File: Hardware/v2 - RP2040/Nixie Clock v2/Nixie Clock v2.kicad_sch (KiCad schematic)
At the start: 25 parts, among them J1 USB_C_Receptacle_USB2.0, J2 Conn_01x03, SW1 SW_Push, U1 RP2040, U2 W25Q128JVS, Y1 12MHz

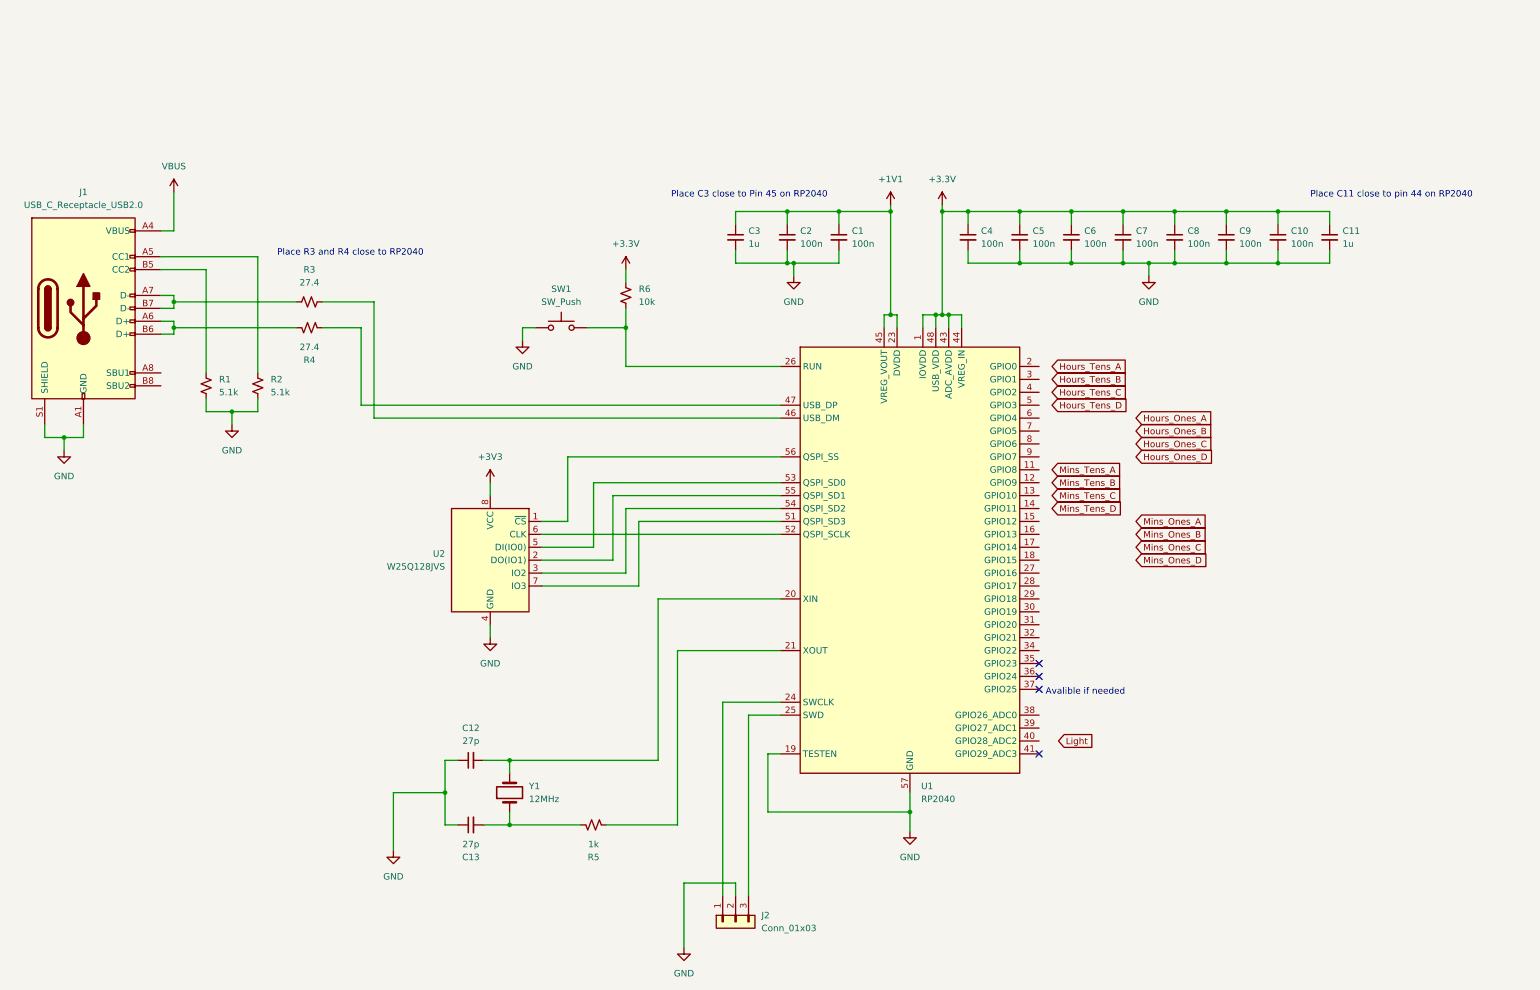
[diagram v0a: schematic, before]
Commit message: added schematic pages and HV switching circuit
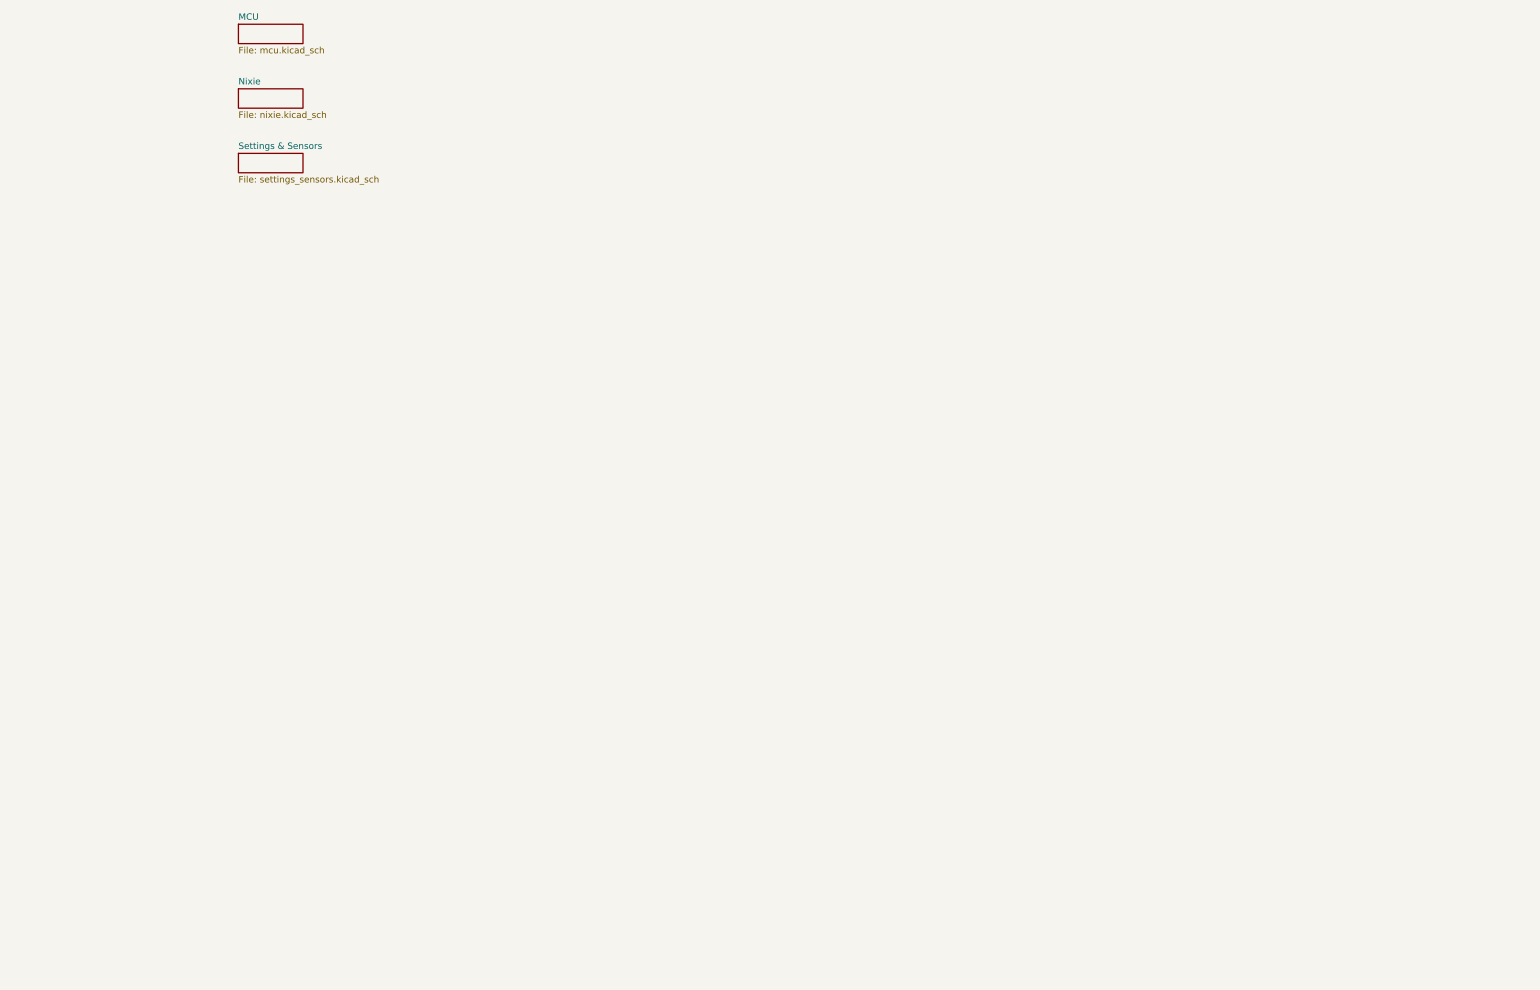
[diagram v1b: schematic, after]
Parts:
- removed C1, C10, C2, C4, C5, C6, C7, C8, C9: 100n, symbol Device:C_Small
- removed C11, C3: 1u, symbol Device:C_Small
- removed C12, C13: 27p, symbol Device:C_Small
- removed J1: USB_C_Receptacle_USB2.0, symbol Connector:USB_C_Receptacle_USB2.0
- removed J2: Conn_01x03, symbol Connector_Generic:Conn_01x03
- removed R1, R2: 5.1k, symbol Device:R_Small_US
- removed R3, R4: 27.4, symbol Device:R_Small_US
- removed R5: 1k, symbol Device:R_Small_US
- removed R6: 10k, symbol Device:R_Small_US
- removed SW1: SW_Push, symbol Switch:SW_Push
- removed U1: RP2040, Package_DFN_QFN:QFN-56-1EP_7x7mm_P0.4mm_EP3.2x3.2mm, symbol MCU_RaspberryPi:RP2040
- removed U2: W25Q128JVS, Package_SO:SOIC-8_5.23x5.23mm_P1.27mm, symbol Memory_Flash:W25Q128JVS
- removed Y1: 12MHz, symbol Device:Crystal
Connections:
- no-connect marks 4 -> 0
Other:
- added sheet MCU (mcu.kicad_sch)
- added sheet Nixie (nixie.kicad_sch)
- added sheet Settings & Sensors (settings_sensors.kicad_sch)
- note removed: "Avalible if needed"
- note removed: "Place C11 close to pin 44 on RP2040"
- note removed: "Place C3 close to Pin 45 on RP2040"
- note removed: "Place R3 and R4 close to RP2040"
- title: (none) -> Nixie Tube Clock

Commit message: Complteted schematic, mergerd schematic on to one sheet, started assigning footprints
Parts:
- added BT1: CR1220, Battery:BatteryHolder_LINX_BAT-HLD-012-SMT, symbol Device:Battery_Cell
- added C10, C11, C12, C13, C14, C15, C16, C17, C20, C21, C24, C25, C29, C3, C33, C35, C5, C9: 100n, Capacitor_SMD:C_0603_1608Metric, symbol Device:C_Small
- added C14: 100u, Capacitor_SMD:C_0603_1608Metric, symbol Device:C_Small
- added C15: 4.7u, Capacitor_THT:CP_Radial_D8.0mm_P3.50mm, symbol Device:C_Polarized_Small_US
- added C18, C19: 1u, Capacitor_SMD:C_0402_1005Metric, symbol Device:C_Small
- added C22, C23, C30, C31, C34: 1u, Capacitor_SMD:C_0603_1608Metric, symbol Device:C_Small
- added C26, C4: 10u, Capacitor_SMD:C_0603_1608Metric, symbol Device:C_Small
- added C27, C28: 27p, Capacitor_SMD:C_0603_1608Metric, symbol Device:C_Small
- added C32: 10n, Capacitor_SMD:C_0603_1608Metric, symbol Device:C_Small
- added C6: 82p, Capacitor_SMD:C_0603_1608Metric, symbol Device:C_Small
- added C7: 33n, Capacitor_SMD:C_0603_1608Metric, symbol Device:C_Small
- added C8: 47u, Capacitor_SMD:C_0603_1608Metric, symbol Device:C_Small
- added J2: USB_C_Receptacle_USB2.0, Connector_USB:USB_C_Receptacle_HRO_TYPE-C-31-M-12, symbol Connector:USB_C_Receptacle_USB2.0
- added J3, J4: Conn_01x03_2.54mm, Connector_PinHeader_2.54mm:PinHeader_1x03_P2.54mm_Vertical, symbol Connector_Generic:Conn_01x03
- added J4: Conn_02x02_2.54mm, Connector_PinHeader_2.54mm:PinHeader_2x02_P2.54mm_Vertical, symbol Connector_Generic:Conn_02x02_Odd_Even
- added JP1, JP2: SolderJumper_2_Open, Jumper:SolderJumper-2_P1.3mm_Open_TrianglePad1.0x1.5mm, symbol Jumper:SolderJumper_2_Open
- added L1: 7.8u, Inductor_SMD:L_Vishay_IHLP-5050, symbol Device:L
- added N1, N2, N3, N4: ИN-8, symbol 0_My_Symbols:ИN-8
- added Q1, Q3: PZTA92, Package_TO_SOT_SMD:SOT-223-3_TabPin2, symbol Transistor_BJT:PZTA92
- added Q2, Q4: MMBTA42, Package_TO_SOT_SMD:SOT-23, symbol Transistor_BJT:MMBTA42
- added R10, R15, R16, R18, R23, R24, R26, R27, R28, R29, R30, R31: 10k, Resistor_SMD:R_0603_1608Metric, symbol Device:R_Small_US
- added R11: 150, Resistor_SMD:R_0603_1608Metric, symbol Device:R_Small_US
- added R12, R13, R14, R23, R24, R25: 100k, Resistor_SMD:R_0603_1608Metric, symbol Device:R_Small_US
- added R17: 30.9, Resistor_SMD:R_0603_1608Metric, symbol Device:R_Small_US
- added R17, R18, R19, R20: 22k, Resistor_SMD:R_0805_2012Metric, symbol Device:R_Small_US
- added R19, R20: 27.4, Resistor_SMD:R_0402_1005Metric, symbol Device:R_Small_US
- added R21, R22: 5.1k, Resistor_SMD:R_0603_1608Metric, symbol Device:R_Small_US
- added R21, R22: 220k, Resistor_SMD:R_0805_2012Metric, symbol Device:R_Small_US
- added R25, R27: 1k, Resistor_SMD:R_0603_1608Metric, symbol Device:R_Small_US
- added R28, R30: 2.2k, Resistor_SMD:R_0603_1608Metric, symbol Device:R_Small_US
- added R9: R_Photo, Resistor_SMD:R_0603_1608Metric, symbol Device:R_Photo
- added SW1, SW2, SW4: SW_Push, symbol Switch:SW_Push
- added SW3: SW_DIP_x10, Button_Switch_SMD:SW_DIP_SPSTx10_Slide_6.7x26.96mm_W6.73mm_P2.54mm_LowProfile_JPin, symbol Switch:SW_DIP_x10
- added U10: W25Q128JVP, Package_SON:WSON-8-1EP_6x5mm_P1.27mm_EP3.4x4.3mm, symbol Memory_Flash:W25Q32JVZP
- added U10: 74LVC1GU04DRL, Package_TO_SOT_SMD:SOT-553, symbol 74xGxx:74LVC1GU04DRL
- added U11: L80-M39, symbol 0_My_Symbols:L80-M39
- added U12: TPS62933, Package_TO_SOT_SMD:SOT-583-8, symbol Regulator_Switching:TPS62933
- added U13: TC2185-3.3VCTTR, Package_TO_SOT_SMD:SOT-23-5, symbol Regulator_Linear:TC2185-3.3VxCTTR
- added U14: AP22913, Package_TO_SOT_SMD:SOT-23-6, symbol 0_My_Symbols:AP22913
- added U14: MCP23017_SS, Package_SO:SSOP-28_5.3x10.2mm_P0.65mm, symbol Interface_Expansion:MCP23017_SS
- added U3, U4, U5, U6: К155ИД1, Package_DIP:DIP-16_W7.62mm, symbol 0_My_Symbols:К155ИД1
- added U7: NCH8200HV, symbol 0_My_Symbols:NCH8200HV
- added U9: RP2040, Package_DFN_QFN:QFN-56-1EP_7x7mm_P0.4mm_EP3.2x3.2mm, symbol MCU_RaspberryPi:RP2040
- added U9: DS3231MZ, Package_SO:SOIC-8_3.9x4.9mm_P1.27mm, symbol Timer_RTC:DS3231MZ
- added Y1: 12MHz, symbol Device:Crystal
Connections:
- new net: R20.1, U9.47 (USB_DP)
- new net: J2.A6 (D+), J2.B6 (D+), R20.2
- new net: SW4.1, U14.23 (GPA2)
- new net: C23.1, C24.1, C25.1, C26.1, R31.1, U11.4 (VCC), U11.5 (V_BCKP), U14.1 (OUT)
- new net: R31.2, U11.10 (~{RESET})
- new net: R10.1, R11.1, R9.2
- new net: JP1.1 (A), Q1.2 (C), R17.1, R18.1, R21.1
- new net: JP1.2 (B), Q3.2 (C), R19.1, R20.1, R22.1
- new net: N2.11 (Anode), R18.2
- new net: N1.1, U3.15 (1)
- new net: N1.10 (0), U3.16 (0)
- new net: N1.11 (Anode), R17.2
- new net: N1.2, U3.8 (2)
- new net: N1.3, U3.9 (3)
- new net: N1.4, U3.13 (4)
- new net: N1.5, U3.14 (5)
- new net: N1.6, U3.11 (6)
- new net: N1.7, U3.10 (7)
- new net: N1.8, U3.1 (8)
- new net: N1.9, U3.2 (9)
- new net: C21.1, R24.1, R25.2, SW2.2
- new net: J4.4 (Pin_4), R22.2
- new net: R26.1, R27.1, U10.4
- new net: Q4.1 (B), R26.2
- new net: C3.1, U12.6 (BST)
- new net: C3.2, L1.1, U12.5 (SW)
- new net: C27.2, U9.20 (XIN), Y1.2
- new net: N4.11 (Anode), R20.2
- new net: Q3.1 (B), R23.2, R24.1
- new net: R24.2, R25.1
- new net: SW3.1, U14.1 (GPB0)
- new net: SW3.10, U14.22 (GPA1)
- new net: SW3.2, U14.2 (GPB1)
- new net: SW3.3, U14.3 (GPB2)
- new net: SW3.4, U14.4 (GPB3)
- new net: SW3.5, U14.5 (GPB4)
- new net: SW3.6, U14.6 (GPB5)
- new net: SW3.7, U14.7 (GPB6)
- new net: SW3.8, U14.8 (GPB7)
- new net: SW3.9, U14.21 (GPA0)
- new net: C15.1, JP2.1 (A), Q1.3 (E), R12.1, U7.3 (170V)
- new net: Q1.1 (B), R12.2, R13.1
- new net: Q2.1 (B), R15.2
- new net: Q2.3 (C), R14.2
- new net: R25.1, U10.1 (~{CS}), U9.56 (QSPI_SS)
- new net: U10.2 (DO(IO1)), U9.55 (QSPI_SD1)
- new net: U10.3 (IO2), U9.54 (QSPI_SD2)
- new net: U10.5 (DI(IO0)), U9.53 (QSPI_SD0)
- new net: U10.6 (CLK), U9.52 (QSPI_SCLK)
- new net: U10.7 (IO3), U9.51 (QSPI_SD3)
- new net: J2.B5 (CC2), R21.2
- new net: N2.8, U4.1 (8)
- new net: N2.7, U4.10 (7)
- new net: N2.6, U4.11 (6)
- new net: N2.4, U4.13 (4)
- new net: N2.5, U4.14 (5)
- new net: N2.1, U4.15 (1)
- new net: N2.10 (0), U4.16 (0)
- new net: N2.9, U4.2 (9)
- new net: N2.2, U4.8 (2)
- new net: N2.3, U4.9 (3)
- new net: C6.2, R17.1, R18.2, U12.8 (FB)
- new net: C32.1, U13.4 (BP)
- new net: Q4.3 (C), R25.2
- new net: C20.1, R23.1, SW1.2, U9.26 (RUN)
- new net: N4.8, U6.1 (8)
- new net: N4.7, U6.10 (7)
- new net: N4.6, U6.11 (6)
- new net: N4.4, U6.13 (4)
- new net: N4.5, U6.14 (5)
- new net: N4.1, U6.15 (1)
- new net: N4.10 (0), U6.16 (0)
- new net: N4.9, U6.2 (9)
- new net: N4.2, U6.8 (2)
- new net: N4.3, U6.9 (3)
- new net: R30.2, U14.19 (INTB)
- new net: JP2.2 (B), Q3.3 (E), R23.1
- new net: BT1.1 (+), U9.6 (VBAT)
- new net: J2.A5 (CC1), R22.2
- new net: J2.A7 (D-), J2.B7 (D-), R19.2
- new net: R27.1, U9.21 (XOUT)
- new net: J4.1 (Pin_1), U9.24 (SWCLK)
- new net: J4.3 (Pin_3), U9.25 (SWD)
- new net: R19.1, U9.46 (USB_DM)
- new net: R28.2, U14.18 (~{RESET})
- new net: N3.1, U5.15 (1)
- new net: N3.10 (0), U5.16 (0)
- new net: N3.11 (Anode), R19.2
- new net: N3.2, U5.8 (2)
- new net: N3.3, U5.9 (3)
- new net: N3.4, U5.13 (4)
- new net: N3.5, U5.14 (5)
- new net: N3.6, U5.11 (6)
- new net: N3.7, U5.10 (7)
- new net: N3.8, U5.1 (8)
- new net: N3.9, U5.2 (9)
- new net: C28.2, R27.2, Y1.1
- new net: R13.2, R14.1
- new net: C7.1, U12.7 (SS)
- new net: J4.2 (Pin_2), R21.2
- new net +1V1: C10.1, C18.1, C9.1, U9.23 (DVDD), U9.45 (VREG_VOUT), U9.50 (DVDD)
- new net +3.3V: C11.1, C12.1, C13.1, C14.1, C15.1, C16.1, C17.1, C19.1, C6.1, C8.1, L1.2, R17.2, R23.2, R24.2, U10.5 (VCC), U9.1 (IOVDD), U9.10 (IOVDD), U9.22 (IOVDD), U9.33 (IOVDD), U9.42 (IOVDD), U9.43 (ADC_AVDD), U9.44 (VREG_IN), U9.48 (USB_VDD), U9.49 (IOVDD)
- new net +3.3VA: C30.1, R9.1, U13.5 (VOUT)
- new net +3V3: C22.1, C29.1, C33.1, R28.1, R28.1, R29.1, R30.1, R30.1, U10.8 (VCC), U14.4 (VIN), U14.6 (VIN), U14.9 (VDD), U9.2 (VCC), U9.4 (~{RST})
- new net Dimming: R15.1, R16.1, U10.2, U9.34 (GPIO22)
- new net GND: BT1.2 (-), C10.2, C11.2, C12.2, C13.2, C14.2, C14.2, C15.2, C15.2, C16.2, C17.2, C18.2, C19.2, C20.2, C21.2, C22.2, C23.2, C24.2, C25.2, C26.2, C27.1, C28.1, C29.2, C30.2, C31.2, C32.2, C33.2, C34.2, C35.1, C35.2, C4.2, C5.2, C7.2, C8.2, C9.2, J2.A1 (GND), J2.A12 (GND), J2.B1 (GND), J2.B12 (GND), J2.S1 (SHIELD), J3.1 (Pin_1), J4.1 (Pin_1), J4.2 (Pin_2), J4.3 (Pin_3), Q2.2 (E), Q4.2 (E), R10.2, R16.2, R18.1, R21.1, R22.1, R27.2, SW1.1, SW2.1, SW3.11, SW3.12, SW3.13, SW3.14, SW3.15, SW3.16, SW3.17, SW3.18, SW3.19, SW3.20, SW4.2, U10.3 (GND), U10.4 (GND), U10.9 (EP), U11.12 (GND), U11.3 (GND), U11.7 (TIMER), U12.4 (GND), U13.2 (GND), U14.10 (VSS), U14.15 (A0), U14.16 (A1), U14.17 (A2), U14.2 (GND), U14.5 (GND), U3.12 (GND), U4.12 (GND), U5.12 (GND), U6.12 (GND), U7.2 (GND), U7.4 (GND), U9.19 (TESTEN), U9.5 (GND), U9.57 (GND)
- new net GPS_EN: U14.3 (EN), U9.35 (GPIO23)
- new net Hours_Ones_A: U4.3 (A), U9.13 (GPIO10)
- new net Hours_Ones_B: U4.6 (B), U9.14 (GPIO11)
- new net Hours_Ones_C: U4.7 (C), U9.15 (GPIO12)
- new net Hours_Ones_D: U4.4 (D), U9.16 (GPIO13)
- new net Hours_Tens_A: U3.3 (A), U9.4 (GPIO2)
- new net Hours_Tens_B: U3.6 (B), U9.5 (GPIO3)
- new net Hours_Tens_C: U3.7 (C), U9.8 (GPIO6)
- new net Hours_Tens_D: U3.4 (D), U9.9 (GPIO7)
- new net I2C0 SCL: R28.2, U14.12 (SCK), U9.7 (GPIO5), U9.8 (SCL)
- new net I2C0_SDA: R30.2, U14.13 (SDA), U9.6 (GPIO4), U9.7 (SDA)
- new net Light: C34.1, R11.2, U9.38 (GPIO26_ADC0)
- new net Mins_Ones_A: U6.3 (A), U9.29 (GPIO18)
- new net Mins_Ones_B: U6.6 (B), U9.30 (GPIO19)
- new net Mins_Ones_C: U6.7 (C), U9.31 (GPIO20)
- new net Mins_Ones_D: U6.4 (D), U9.32 (GPIO21)
- new net Mins_Tens_A: U5.3 (A), U9.17 (GPIO14)
- new net Mins_Tens_B: U5.6 (B), U9.18 (GPIO15)
- new net Mins_Tens_C: U5.7 (C), U9.27 (GPIO16)
- new net Mins_Tens_D: U5.4 (D), U9.28 (GPIO17)
- new net RTC_Interrupt: U9.3 (~{INT}/SQW), U9.36 (GPIO24)
- new net Settings_Interrupt: R29.2, U14.20 (INTA), U9.37 (GPIO25)
- new net UART0 RX: J3.2 (Pin_2), U9.3 (GPIO1)
- new net UART0 TX: J3.3 (Pin_3), U9.2 (GPIO0)
- new net UART1_RX: U11.2 (TXD1), U9.12 (GPIO9)
- new net UART1_TX: U11.1 (RXD1), U9.11 (GPIO8)
- new net VBUS: C14.1, C31.1, C4.1, C5.1, J2.A4 (VBUS), J2.A9 (VBUS), J2.B4 (VBUS), J2.B9 (VBUS), U12.3 (VIN), U13.1 (VIN), U13.3 (ON/~{OFF}), U3.5 (Vcc), U4.5 (Vcc), U5.5 (Vcc), U6.5 (Vcc), U7.1 (Vin)
- no-connect marks 0 -> 11
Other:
- removed sheet MCU
- removed sheet Nixie
- removed sheet Settings & Sensors
- note added: "1060Hz LPF Sample at <= 530Hz or 1.89ms"
- note added: "128MBit / 16MB Flash"
- note added: "250V or larger"
- note added: "3.3V REGULATOR"
- note added: "Close either JP1 OR JP2, NOT BOTH. Close JP1 for 1 switching circuit Close JP2 for 2 switching circuits"
- note added: "Colon mounting point"
- note added: "DNP Might be needed to balance load on power supply"
- note added: "Debug UART"
- note added: "GPS"
- note added: "High side switch"
- note added: "IO EXPANDER FOR SETTINGS"
- note added: "LIGHT SENSOR"
- note added: "Linear supply for analog circuits"
- note added: "Low ESR"
- note added: "NIXIE TUBES"
- note added: "Place C11 close to pin 44 on RP2040"
- note added: "Place C3 close to Pin 45 on RP2040"
- note added: "Place R3 and R4 close to RP2040"
- note added: "RTC"
- note added: "Reset"
- note added: "SETTINGS KEY 1) DST 2) 12/24HR 3) +/- 4) 8 5) 4 6) 2 7) 1 8) +00:30 9) +00:45 10) UNUSED"
- note added: "SW Debug"
- note added: "Submit settings"
- note added: "This is probably an overkill ammount of storeage for this. I may decrease it latter."
- note added: "USB Boot"
- note added: "Vin to 3.3V"

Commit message: Finished assigning footprints and started layout
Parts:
- removed Y1: 12MHz, symbol Device:Crystal
- added Y1: 12MHz, 0_My_Footprints:Crystal_SMD_Abracon_ABM10-4Pin_2.5x2.0mm, symbol Device:Crystal_GND24
- C27, C28: value 27p -> 8p; footprint Capacitor_SMD:C_0603_1608Metric -> Capacitor_SMD:C_0402_1005Metric
- N1, N2, N3, N4: footprint (none) -> Display_Nixie:ИN-8 DSUB
- R27: footprint Resistor_SMD:R_0603_1608Metric -> Resistor_SMD:R_0402_1005Metric
- SW1, SW2, SW4: footprint (none) -> Button_Switch_SMD:SW_Push_1P1T_NO_CK_KMR2; MPN (none) -> KMR213G LFG
- U1: renamed from U7; footprint (none) -> Display_Nixie:NCH8200HV
- U11: footprint (none) -> RF_GPS:Quectel_L80-R
- renumbered C14 to C1, C15 to C2, J4 to J1, JP2 to JP1, JP1 to JP2, Q3 to Q2, Q2 to Q3, R12 to R1, R27 to R10, R17 to R11, R18 to R12, R21 to R13, R22 to R14, R19 to R15, R20 to R16, R23 to R2, R31 to R26, R30 to R28, R28 to R29, R13 to R3, R29 to R30, R30 to R31, R28 to R32, R9 to R33, R11 to R34, R10 to R35, R24 to R4, R14 to R5, R25 to R6, R15 to R7, R26 to R8, R16 to R9, U9 to U12, U10 to U2, U12 to U3, U3 to U4, U4 to U5, U5 to U6, U6 to U7, U14 to U8
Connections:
- net GND: now also Y1.2, Y1.4
- net at C27.2, U9.20 (XIN): now also Y1.1
- net at C28.2, R27.2: now also Y1.3
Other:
- moved on the sheet: BT1, C1, C10, C11, C12, C13, C14, C15, C16, C17, C18, C19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

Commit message: Continued work on layout
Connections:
- net GND: no longer C35.1
- net at SW4.1, U14.23 (GPA2): now also C35.1
- net ANODE_1: now reaches JP2.1 (A), Q1.2 (C), R11.1, R12.1, R13.1
- net ANODE_2: now reaches JP2.2 (B), Q2.2 (C), R14.1, R15.1, R16.1
- net 170V_1: now reaches C2.1, JP1.1 (A), Q1.3 (E), R1.1, U1.3 (170V)
- net 170V_2: now reaches JP1.2 (B), Q2.3 (E), R2.1
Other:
- moved on the sheet: C35, R26
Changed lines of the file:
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@@
   (junction (at 441.96 66.04) (diameter 0) (color 0 0 0 0)
   )
-  (junction (at 575.31 538.48) (diameter 0) (color 0 0 0 0)
-  )
   (junction (at 576.58 488.95) (diameter 0) (color 0 0 0 0)
   )
@@
   (junction (at 317.5 241.3) (diameter 0) (color 0 0 0 0)
   )
+  (junction (at 557.53 538.48) (diameter 0) (color 0 0 0 0)
+  )
   (junction (at 494.03 527.05) (diameter 0) (color 0 0 0 0)
   )
@@
     (stroke (width 0) (type default))
   )
-  (wire (pts (xy 575.31 538.48) (xy 575.31 541.02))
-    (stroke (width 0) (type default))
-  )
   (wire (pts (xy 198.12 179.07) (xy 203.2 179.07))
     (stroke (width 0) (type default))
@@
     (stroke (width 0) (type default))
   )
-  (wire (pts (xy 575.31 538.48) (xy 585.47 538.48))
-    (stroke (width 0) (type default))
-  )
   (wire (pts (xy 295.91 331.47) (xy 364.49 331.47))
     (stroke (width 0) (type default))
@@
     (stroke (width 0) (type default))
   )
-  (wire (pts (xy 572.77 538.48) (xy 575.31 538.48))
+  (wire (pts (xy 572.77 538.48) (xy 585.47 538.48))
     (stroke (width 0) (type default))
   )
@@
     (stroke (width 0) (type default))
   )
-  (wire (pts (xy 501.65 350.52) (xy 533.4 350.52))
+  (wire (pts (xy 514.35 350.52) (xy 533.4 350.52))
     (stroke (width 0) (type default))
   )
@@
     (stroke (width 0) (type default))
   )
-  (wire (pts (xy 501.65 351.79) (xy 501.65 350.52))
+  (wire (pts (xy 514.35 356.87) (xy 514.35 350.52))
     (stroke (width 0) (type default))
   )
@@
     (stroke (width 0) (type default))
   )
-  (wire (pts (xy 523.24 375.92) (xy 501.65 375.92))
+  (wire (pts (xy 523.24 375.92) (xy 514.35 375.92))
     (stroke (width 0) (type default))
   )
@@
     (stroke (width 0) (type default))
   )
-  (wire (pts (xy 501.65 375.92) (xy 501.65 356.87))
+  (wire (pts (xy 514.35 375.92) (xy 514.35 361.95))
     (stroke (width 0) (type default))
   )
@@
     (stroke (width 0) (type default))
   )
+  (wire (pts (xy 557.53 538.48) (xy 557.53 541.02))
+    (stroke (width 0) (type default))
+  )
   (wire (pts (xy 270.51 374.65) (xy 270.51 378.46))
     (stroke (width 0) (type default))
@@
     (stroke (width 0) (type default))
   )
-  (wire (pts (xy 575.31 548.64) (xy 585.47 548.64))
+  (wire (pts (xy 557.53 548.64) (xy 585.47 548.64))
     (stroke (width 0) (type default))
   )
@@
     (stroke (width 0) (type default))
   )
-  (wire (pts (xy 575.31 546.1) (xy 575.31 548.64))
+  (wire (pts (xy 557.53 546.1) (xy 557.53 548.64))
     (stroke (width 0) (type default))
   )
@@
     (effects (font (size 1.27 1.27)) (justify left bottom))
   )
+  (label "170V_1" (at 450.85 66.04 0) (fields_autoplaced)
+    (effects (font (size 1.27 1.27)) (justify left bottom))
+  )
   (label "Mins_Ones_B" (at 704.85 261.62 90) (fields_autoplaced)
     (effects (font (size 1.27 1.27)) (justify left bottom))
@@
     (effects (font (size 1.27 1.27)) (justify left bottom))
   )
+  (label "170V_2" (at 539.75 66.04 0) (fields_autoplaced)
+    (effects (font (size 1.27 1.27)) (justify left bottom))
+  )
   (label "Hours_Ones_B" (at 527.05 261.62 90) (fields_autoplaced)
     (effects (font (size 1.27 1.27)) (justify left bottom))
@@
     (effects (font (size 1.27 1.27)) (justify left bottom))
   )
+  (label "ANODE_1" (at 499.11 116.84 90) (fields_autoplaced)
+    (effects (font (size 1.27 1.27)) (justify left bottom))
+  )
   (label "RTC_Interrupt" (at 331.47 351.79 0) (fields_autoplaced)
     (effects (font (size 1.27 1.27)) (justify left bottom))
@@
     (effects (font (size 1.27 1.27)) (justify left bottom))
   )
+  (label "ANODE_2" (at 607.06 116.84 90) (fields_autoplaced)
+    (effects (font (size 1.27 1.27)) (justify left bottom))
+  )
   (label "Hours_Ones_D" (at 532.13 261.62 90) (fields_autoplaced)
     (effects (font (size 1.27 1.27)) (justify left bottom))
@@
     )
   )
-  (symbol (lib_id "Device:R_Small_US") (at 501.65 354.33 0) (mirror y) (unit 1)
+  (symbol (lib_id "Device:R_Small_US") (at 514.35 359.41 0) (mirror y) (unit 1)
     (in_bom yes) (on_board yes) (dnp no) (fields_autoplaced)
-    (property "Reference" "R26" (at 499.11 353.06 0)
+    (property "Reference" "R26" (at 511.81 358.14 0)
       (effects (font (size 1.27 1.27)) (justify left))
     )
-    (property "Value" "10k" (at 499.11 355.6 0)
+    (property "Value" "10k" (at 511.81 360.68 0)
       (effects (font (size 1.27 1.27)) (justify left))
     )
-    (property "Footprint" "Resistor_SMD:R_0603_1608Metric" (at 501.65 354.33 0)
+    (property "Footprint" "Resistor_SMD:R_0603_1608Metric" (at 514.35 359.41 0)
       (effects (font (size 1.27 1.27)) hide)
     )
-    (property "Datasheet" "~" (at 501.65 354.33 0)
+    (property "Datasheet" "~" (at 514.35 359.41 0)
       (effects (font (size 1.27 1.27)) hide)
     )
@@
     )
   )
-  (symbol (lib_id "Device:C_Small") (at 575.31 543.56 0) (unit 1)
+  (symbol (lib_id "Device:C_Small") (at 557.53 543.56 0) (unit 1)
     (in_bom yes) (on_board yes) (dnp no) (fields_autoplaced)
-    (property "Reference" "C35" (at 577.85 542.2963 0)
+    (property "Reference" "C35" (at 560.07 542.2963 0)
       (effects (font (size 1.27 1.27)) (justify left))
     )
-    (property "Value" "100n" (at 577.85 544.8363 0)
+    (property "Value" "100n" (at 560.07 544.8363 0)
       (effects (font (size 1.27 1.27)) (justify left))
     )
-    (property "Footprint" "Capacitor_SMD:C_0603_1608Metric" (at 575.31 543.56 0)
+    (property "Footprint" "Capacitor_SMD:C_0603_1608Metric" (at 557.53 543.56 0)
       (effects (font (size 1.27 1.27)) hide)
     )
-    (property "Datasheet" "~" (at 575.31 543.56 0)
+    (property "Datasheet" "~" (at 557.53 543.56 0)
       (effects (font (size 1.27 1.27)) hide)
     )
@@
     (pin "7")
     (pin "8")
+    (pin "9")
     (instances
       (project "Nixie Clock v2"
